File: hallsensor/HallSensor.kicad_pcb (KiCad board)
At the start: 2 copper layers, 6.3 x 20.3 mm, 5 parts

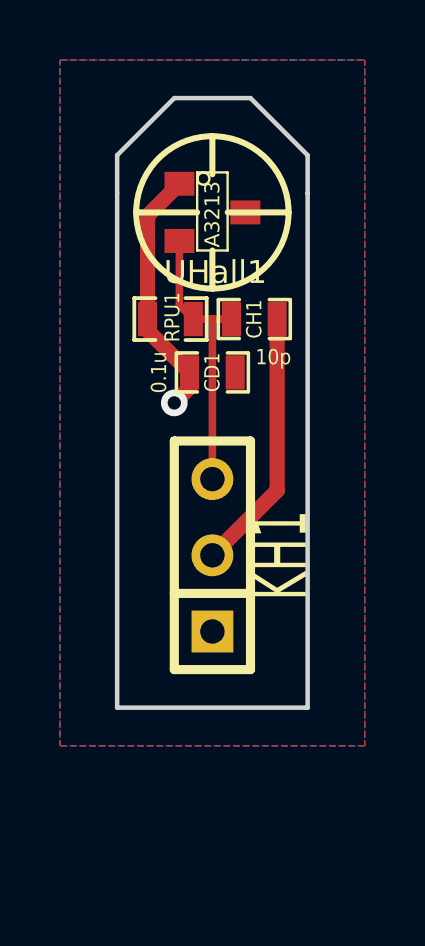
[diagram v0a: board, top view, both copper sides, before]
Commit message: Revised copper pour and and routing.
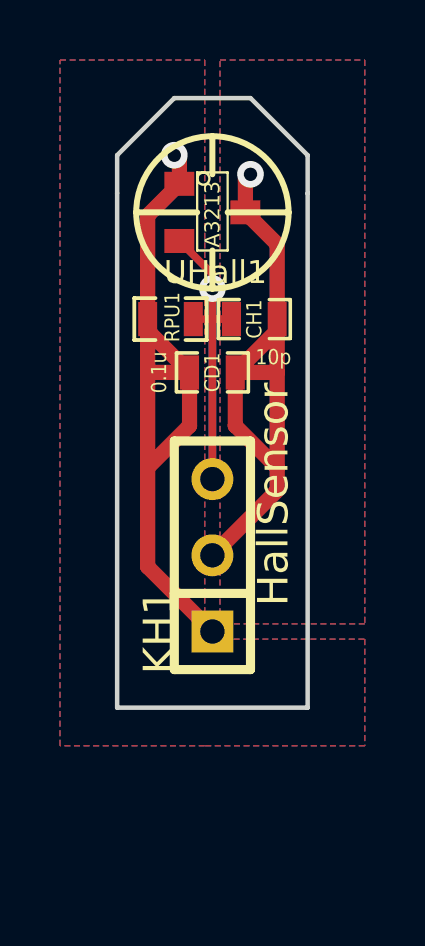
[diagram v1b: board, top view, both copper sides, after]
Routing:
- net VCC: track 8.53 -> 24.8 mm
- net VSS: track 8.77 -> 21.6 mm, vias 0 -> 1
- net /hall1: track 9.40 -> 16.0 mm, vias 0 -> 1
- added copper zone on F.Cu, net VCC
- added copper zone on B.Cu, net VSS
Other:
- board text added: "ClothBot Designs"
- board text added: "HallSensor"

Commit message: Added alignment vias at +/-0.1"
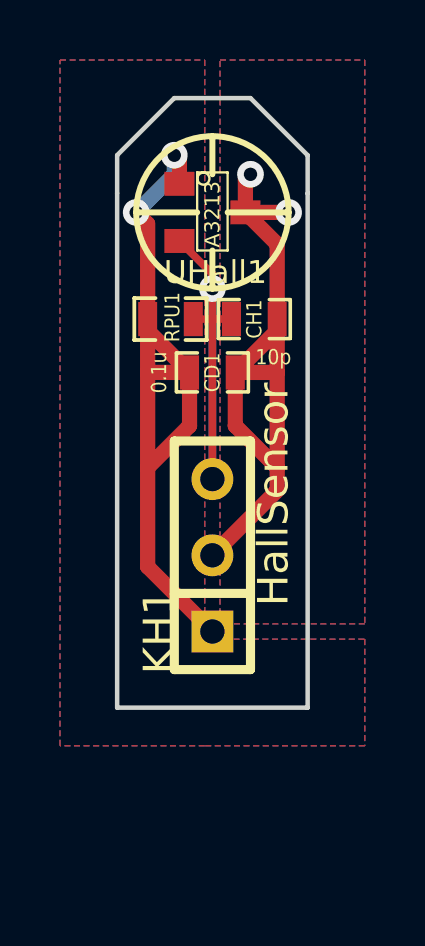
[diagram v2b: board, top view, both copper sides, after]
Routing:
- net VSS: track 21.6 -> 23.1 mm, vias 1 -> 2
- net VCC: track 24.8 -> 26.0 mm, vias 1 -> 2
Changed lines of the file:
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@@
-(kicad_pcb (version 3) (host pcbnew "(2013-09-28 BZR 4356)-product")
+(kicad_pcb (version 3) (host pcbnew "(2013-mar-25)-stable")
   (general
     (links 9)
     (no_connects 0)
-    (area 11.059524 17.610001 30.480001 43.180001)
+    (area 11.059524 17.610001 31.62179 43.180001)
     (thickness 1.6)
     (drawings 20)
-    (tracks 36)
+    (tracks 41)
     (zones 0)
     (modules 5)
@@
   (layers
     (15 F.Cu signal)
-    (0 B.Cu signal)
+    (0 B.Cu signal hide)
     (16 B.Adhes user)
     (17 F.Adhes user)
@@
       (usegerberextensions true)
       (excludeedgelayer true)
-      (linewidth 0.150000)
+      (linewidth 0)
       (plotframeref false)
       (viasonmask false)
@@
     (fp_line (start 1.27 0.508) (end -1.3335 0.508) (layer F.SilkS) (width 0.07874))
     (fp_line (start -1.3335 -0.508) (end 1.27 -0.508) (layer F.SilkS) (width 0.07874))
-    (pad 2 smd rect (at 0 -1.09982 270) (size 0.8001 1.00076) (layers F.Cu F.Paste F.Mask)
-      (net 3 VSS))
-    (pad 3 smd rect (at 0.9525 1.09982 270) (size 0.8001 1.00076) (layers F.Cu F.Paste F.Mask)
-      (net 1 /hall1))
-    (pad 1 smd rect (at -0.9525 1.09982 270) (size 0.8001 1.00076) (layers F.Cu F.Paste F.Mask)
-      (net 2 VCC))
+    (pad 2 smd rect (at 0 -1.09982 270) (size 0.8001 1.00076)
+      (layers F.Cu F.Paste F.Mask)
+      (net 3 VSS)
+    )
+    (pad 3 smd rect (at 0.9525 1.09982 270) (size 0.8001 1.00076)
+      (layers F.Cu F.Paste F.Mask)
+      (net 1 /hall1)
+    )
+    (pad 1 smd rect (at -0.9525 1.09982 270) (size 0.8001 1.00076)
+      (layers F.Cu F.Paste F.Mask)
+      (net 2 VCC)
+    )
     (model smd\SOT23_3.wrl
       (at (xyz 0 0 0))
@@
     (fp_line (start 1.19888 -0.635) (end 1.19888 0.635) (layer F.SilkS) (width 0.11938))
     (fp_line (start -1.19888 0.635) (end -1.19888 -0.635) (layer F.SilkS) (width 0.11938))
-    (pad 1 smd rect (at -0.762 0) (size 0.635 1.143) (layers F.Cu F.Paste F.Mask)
-      (net 2 VCC))
-    (pad 2 smd rect (at 0.762 0) (size 0.635 1.143) (layers F.Cu F.Paste F.Mask)
-      (net 3 VSS))
+    (pad 1 smd rect (at -0.762 0) (size 0.635 1.143)
+      (layers F.Cu F.Paste F.Mask)
+      (net 2 VCC)
+    )
+    (pad 2 smd rect (at 0.762 0) (size 0.635 1.143)
+      (layers F.Cu F.Paste F.Mask)
+      (net 3 VSS)
+    )
     (model smd\capacitors\C0603.wrl
       (at (xyz 0 0 0.001))
@@
     (fp_line (start 1.19888 -0.635) (end 1.19888 0.635) (layer F.SilkS) (width 0.11938))
     (fp_line (start -1.19888 0.635) (end -1.19888 -0.635) (layer F.SilkS) (width 0.11938))
-    (pad 1 smd rect (at -0.762 0) (size 0.635 1.143) (layers F.Cu F.Paste F.Mask)
-      (net 1 /hall1))
-    (pad 2 smd rect (at 0.762 0) (size 0.635 1.143) (layers F.Cu F.Paste F.Mask)
-      (net 3 VSS))
+    (pad 1 smd rect (at -0.762 0) (size 0.635 1.143)
+      (layers F.Cu F.Paste F.Mask)
+      (net 1 /hall1)
+    )
+    (pad 2 smd rect (at 0.762 0) (size 0.635 1.143)
+      (layers F.Cu F.Paste F.Mask)
+      (net 3 VSS)
+    )
     (model smd\capacitors\C0603.wrl
       (at (xyz 0 0 0.001))
@@
     (fp_line (start 3.81 1.27) (end -3.81 1.27) (layer F.SilkS) (width 0.3048))
     (fp_line (start -1.27 -1.27) (end -1.27 1.27) (layer F.SilkS) (width 0.3048))
-    (pad 1 thru_hole rect (at -2.54 0 90) (size 1.397 1.397) (drill 0.8128) (layers *.Cu *.Mask F.SilkS)
-      (net 2 VCC))
-    (pad 2 thru_hole circle (at 0 0 90) (size 1.397 1.397) (drill 0.8128) (layers *.Cu *.Mask F.SilkS)
-      (net 3 VSS))
-    (pad 3 thru_hole circle (at 2.54 0 90) (size 1.397 1.397) (drill 0.8128) (layers *.Cu *.Mask F.SilkS)
-      (net 1 /hall1))
+    (pad 1 thru_hole rect (at -2.54 0 90) (size 1.397 1.397) (drill 0.8128)
+      (layers *.Cu *.Mask F.SilkS)
+      (net 2 VCC)
+    )
+    (pad 2 thru_hole circle (at 0 0 90) (size 1.397 1.397) (drill 0.8128)
+      (layers *.Cu *.Mask F.SilkS)
+      (net 3 VSS)
+    )
+    (pad 3 thru_hole circle (at 2.54 0 90) (size 1.397 1.397) (drill 0.8128)
+      (layers *.Cu *.Mask F.SilkS)
+      (net 1 /hall1)
+    )
   )
   (module SM0603_Resistor (layer F.Cu)
@@
     (fp_line (start 1.2065 -0.6985) (end 1.2065 0.6985) (layer F.SilkS) (width 0.127))
     (fp_line (start 1.2065 0.6985) (end 0.50038 0.6985) (layer F.SilkS) (width 0.127))
-    (pad 1 smd rect (at -0.762 0) (size 0.635 1.143) (layers F.Cu F.Paste F.Mask)
-      (net 2 VCC))
-    (pad 2 smd rect (at 0.762 0) (size 0.635 1.143) (layers F.Cu F.Paste F.Mask)
-      (net 1 /hall1))
+    (pad 1 smd rect (at -0.762 0) (size 0.635 1.143)
+      (layers F.Cu F.Paste F.Mask)
+      (net 2 VCC)
+    )
+    (pad 2 smd rect (at 0.762 0) (size 0.635 1.143)
+      (layers F.Cu F.Paste F.Mask)
+      (net 1 /hall1)
+    )
     (model smd\resistors\R0603.wrl
       (at (xyz 0 0 0.001))
@@
   (segment (start 24.765 28.956) (end 25.4 28.956) (width 0.254) (layer F.Cu) (net 1))
   (segment (start 25.4 28.956) (end 26.035 28.956) (width 0.254) (layer F.Cu) (net 1))
+  (segment (start 24.13 23.495) (end 24.13 24.13) (width 0.508) (layer B.Cu) (net 2))
+  (segment (start 24.30018 23.66518) (end 24.13 23.495) (width 0.508) (layer F.Cu) (net 2))
+  (via (at 24.13 23.495) (size 0.889) (layers F.Cu B.Cu) (net 2))
   (segment (start 24.30018 24.4475) (end 24.30018 23.66518) (width 0.508) (layer F.Cu) (net 2))
-  (via (at 24.13 23.495) (size 0.889) (layers F.Cu B.Cu) (net 2))
-  (segment (start 24.30018 23.66518) (end 24.13 23.495) (width 0.508) (layer F.Cu) (net 2))
+  (segment (start 23.241 25.781) (end 22.86 25.4) (width 0.508) (layer F.Cu) (net 2))
+  (via (at 22.86 25.4) (size 0.889) (layers F.Cu B.Cu) (net 2))
+  (segment (start 23.241 25.781) (end 23.241 28.956) (width 0.508) (layer F.Cu) (net 2))
+  (segment (start 24.13 24.13) (end 22.86 25.4) (width 0.508) (layer B.Cu) (net 2))
   (segment (start 23.241 28.956) (end 23.241 29.337) (width 0.508) (layer F.Cu) (net 2))
   (segment (start 23.241 29.337) (end 24.638 30.734) (width 0.508) (layer F.Cu) (net 2))
@@
   (segment (start 23.241 33.909) (end 23.241 37.211) (width 0.508) (layer F.Cu) (net 2))
   (segment (start 23.241 37.211) (end 25.4 39.37) (width 0.508) (layer F.Cu) (net 2))
-  (segment (start 23.241 28.956) (end 23.241 25.50668) (width 0.508) (layer F.Cu) (net 2))
-  (segment (start 23.241 25.50668) (end 24.30018 24.4475) (width 0.508) (layer F.Cu) (net 2))
+  (segment (start 26.49982 25.4) (end 27.94 25.4) (width 0.508) (layer F.Cu) (net 3))
+  (via (at 27.94 25.4) (size 0.889) (layers F.Cu B.Cu) (net 3))
   (segment (start 26.49982 25.4) (end 26.49982 24.30018) (width 0.508) (layer F.Cu) (net 3))
   (via (at 26.67 24.13) (size 0.889) (layers F.Cu B.Cu) (net 3))

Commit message: Misc rework.
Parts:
- removed KH1: CONN_3, SIL-3
- added ANCHOR1: CONN_1, PINTST, F.Cu at (25.4, 22.9)
- added PAIR1: CONN_2, EDGE_2, F.Cu at (24.1, 38.1)
- added PAIR2: CONN_2, EDGE_2, F.Cu at (25.4, 38.1)
- added PAIR3: CONN_2, EDGE_2, F.Cu at (26.7, 38.1)
- moved CD1 0.64 mm to (25.4, 30.1)
- moved CH1 0.63 mm to (26.8, 28.3)
- moved RPU1 0.63 mm to (24.0, 28.3)
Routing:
- net /hall1: track 16.0 -> 23.1 mm, vias 1 -> 3
- net VCC: track 26.0 -> 23.7 mm, vias 2 -> 3
- net VSS: track 23.1 -> 22.8 mm, vias 2 -> 4
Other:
- net class Default: clearance 0.254 -> 0.2032
- net class PWR_Nets: clearance 0.254 -> 0.2032
- rule trace_clearance: 0.254 -> 0.2032

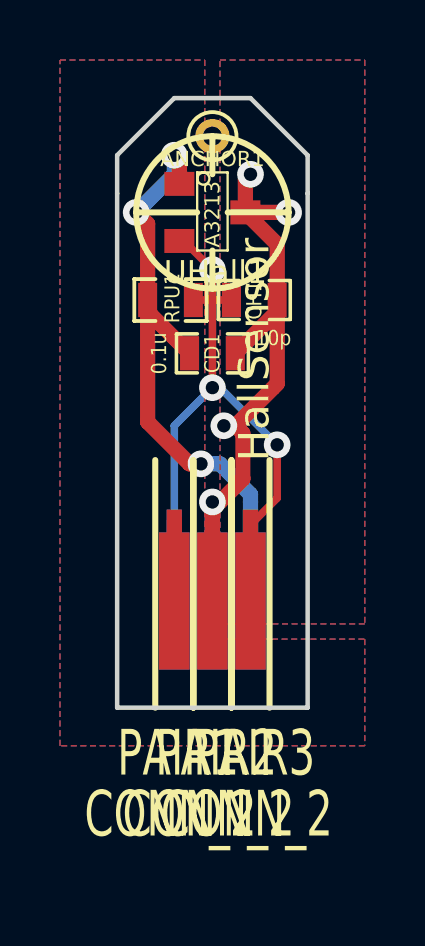
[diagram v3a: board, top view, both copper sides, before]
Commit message: Adjusted EDGE_2 silk layer.
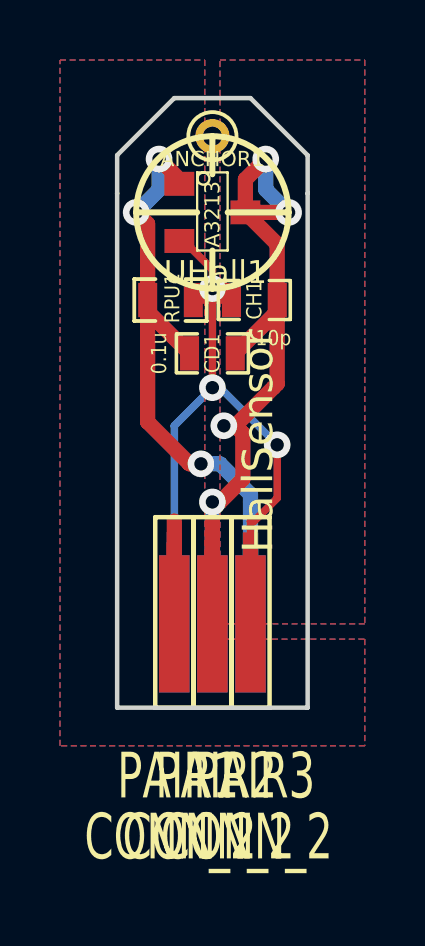
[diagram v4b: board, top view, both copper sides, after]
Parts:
- moved PAIR1 0.76 mm to (24.1, 38.9)
- moved PAIR2 0.76 mm to (25.4, 38.9)
- moved PAIR3 0.76 mm to (26.7, 38.9)
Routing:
- net VSS: track 22.8 -> 31.0 mm
- net /hall1: track 23.1 -> 28.7 mm
- net VCC: track 23.7 -> 28.8 mm
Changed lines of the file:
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@@
     (links 18)
     (no_connects 1)
-    (area 11.059524 17.610001 30.98679 46.5328)
+    (area 11.059524 17.610001 31.11379 47.2948)
     (thickness 1.6)
     (drawings 20)
-    (tracks 62)
+    (tracks 71)
     (zones 0)
     (modules 8)
@@
   )
   (module EDGE_2 (layer F.Cu)
-    (at 25.4 38.1 180)
+    (at 25.4 38.862 180)
     (descr "Edge Connector")
     (tags "EDGE CONN")
@@
       (effects (font (size 1.524 1.016) (thickness 0.2032)))
     )
-    (fp_line (start 0.635 4.445) (end 0.635 -3.81) (layer F.SilkS) (width 0.2032))
-    (fp_line (start -0.635 4.445) (end -0.635 -3.81) (layer F.SilkS) (width 0.2032))
+    (fp_line (start -0.635 3.302) (end 0.635 3.302) (layer F.SilkS) (width 0.15))
+    (fp_line (start 0.635 3.302) (end 0.635 -3.048) (layer F.SilkS) (width 0.15))
+    (fp_line (start 0.635 -3.048) (end -0.635 -3.048) (layer F.SilkS) (width 0.15))
+    (fp_line (start -0.635 -3.048) (end -0.635 3.302) (layer F.SilkS) (width 0.15))
     (pad 1 connect rect (at 0 -0.254 180) (size 1.016 4.572)
       (layers F.Cu F.Mask)
@@
   )
   (module EDGE_2 (layer F.Cu)
-    (at 26.67 38.1 180)
+    (at 26.67 38.862 180)
     (descr "Edge Connector")
     (tags "EDGE CONN")
@@
       (effects (font (size 1.524 1.016) (thickness 0.2032)))
     )
-    (fp_line (start 0.635 4.445) (end 0.635 -3.81) (layer F.SilkS) (width 0.2032))
-    (fp_line (start -0.635 4.445) (end -0.635 -3.81) (layer F.SilkS) (width 0.2032))
+    (fp_line (start -0.635 3.302) (end 0.635 3.302) (layer F.SilkS) (width 0.15))
+    (fp_line (start 0.635 3.302) (end 0.635 -3.048) (layer F.SilkS) (width 0.15))
+    (fp_line (start 0.635 -3.048) (end -0.635 -3.048) (layer F.SilkS) (width 0.15))
+    (fp_line (start -0.635 -3.048) (end -0.635 3.302) (layer F.SilkS) (width 0.15))
     (pad 1 connect rect (at 0 -0.254 180) (size 1.016 4.572)
       (layers F.Cu F.Mask)
@@
   )
   (module EDGE_2 (layer F.Cu)
-    (at 24.13 38.1 180)
+    (at 24.13 38.862 180)
     (descr "Edge Connector")
     (tags "EDGE CONN")
@@
       (effects (font (size 1.524 1.016) (thickness 0.2032)))
     )
-    (fp_line (start 0.635 4.445) (end 0.635 -3.81) (layer F.SilkS) (width 0.2032))
-    (fp_line (start -0.635 4.445) (end -0.635 -3.81) (layer F.SilkS) (width 0.2032))
+    (fp_line (start -0.635 3.302) (end 0.635 3.302) (layer F.SilkS) (width 0.15))
+    (fp_line (start 0.635 3.302) (end 0.635 -3.048) (layer F.SilkS) (width 0.15))
+    (fp_line (start 0.635 -3.048) (end -0.635 -3.048) (layer F.SilkS) (width 0.15))
+    (fp_line (start -0.635 -3.048) (end -0.635 3.302) (layer F.SilkS) (width 0.15))
     (pad 1 connect rect (at 0 -0.254 180) (size 1.016 4.572)
       (layers F.Cu F.Mask)
@@
     )
   )
-  (gr_text "ClothBot Designs" (at 23.622 33.274 90) (layer B.SilkS)
+  (gr_text "ClothBot Designs" (at 23.876 30.226 90) (layer B.SilkS)
     (effects (font (size 1.016 1.016) (thickness 0.2032)) (justify mirror))
   )
-  (gr_text HallSensor (at 26.797 29.972 90) (layer F.SilkS)
+  (gr_text HallSensor (at 26.924 33.02 90) (layer F.SilkS)
     (effects (font (size 1.016 1.016) (thickness 0.2032)))
   )
@@
   (gr_circle (center 25.4 25.4) (end 27.94 25.4) (layer B.SilkS) (width 0.2))
   (gr_circle (center 25.4 25.4) (end 27.94 25.4) (layer F.SilkS) (width 0.2))
+  (segment (start 25.4 28.194) (end 25.4 27.94) (width 0.254) (layer F.Cu) (net 1))
+  (via (at 25.4 27.94) (size 0.889) (layers F.Cu B.Cu) (net 1))
+  (segment (start 26.67 36.449) (end 26.67 39.116) (width 0.254) (layer F.Cu) (net 1))
+  (segment (start 24.13 36.449) (end 24.13 39.116) (width 0.254) (layer B.Cu) (net 1))
   (segment (start 27.559 33.147) (end 25.654 31.242) (width 0.254) (layer B.Cu) (net 1))
   (segment (start 26.67 35.687) (end 26.67 38.354) (width 0.254) (layer F.Cu) (net 1))
@@
   (segment (start 25.4 28.194) (end 25.4 27.305) (width 0.254) (layer F.Cu) (net 1))
   (segment (start 24.4475 26.3525) (end 25.4 27.305) (width 0.254) (layer F.Cu) (net 1))
-  (via (at 25.4 27.305) (size 0.889) (layers F.Cu B.Cu) (net 1))
   (segment (start 24.4475 26.3525) (end 24.30018 26.3525) (width 0.254) (layer F.Cu) (net 1))
   (segment (start 24.765 28.321) (end 25.4 28.321) (width 0.254) (layer F.Cu) (net 1))
   (segment (start 25.4 28.321) (end 26.035 28.321) (width 0.254) (layer F.Cu) (net 1))
+  (segment (start 23.622 23.622) (end 23.622 24.638) (width 0.508) (layer B.Cu) (net 2))
+  (via (at 22.86 25.4) (size 0.889) (layers F.Cu B.Cu) (net 2))
+  (segment (start 23.241 25.781) (end 22.86 25.4) (width 0.508) (layer F.Cu) (net 2))
+  (segment (start 23.241 28.321) (end 23.241 25.781) (width 0.508) (layer F.Cu) (net 2))
+  (segment (start 24.30018 24.30018) (end 23.622 23.622) (width 0.508) (layer F.Cu) (net 2))
+  (via (at 23.622 23.622) (size 0.889) (layers F.Cu B.Cu) (net 2))
+  (segment (start 24.30018 24.30018) (end 24.30018 24.4475) (width 0.508) (layer F.Cu) (net 2))
+  (segment (start 23.622 24.638) (end 22.86 25.4) (width 0.508) (layer B.Cu) (net 2))
+  (segment (start 24.13 36.449) (end 24.13 39.116) (width 0.508) (layer F.Cu) (net 2))
+  (segment (start 26.67 36.449) (end 26.67 39.116) (width 0.508) (layer B.Cu) (net 2))
+  (segment (start 24.13 35.687) (end 24.13 38.354) (width 0.508) (layer F.Cu) (net 2))
   (segment (start 25.019 33.782) (end 25.654 33.782) (width 0.508) (layer B.Cu) (net 2))
   (segment (start 26.67 35.052) (end 26.67 35.687) (width 0.508) (layer B.Cu) (net 2))
   (segment (start 26.67 34.798) (end 26.67 35.052) (width 0.508) (layer B.Cu) (net 2))
   (segment (start 25.654 33.782) (end 26.67 34.798) (width 0.508) (layer B.Cu) (net 2))
-  (segment (start 24.13 35.687) (end 24.13 38.354) (width 0.508) (layer F.Cu) (net 2))
   (segment (start 26.67 35.687) (end 26.67 38.354) (width 0.508) (layer B.Cu) (net 2))
   (segment (start 23.241 32.385) (end 24.638 33.782) (width 0.508) (layer F.Cu) (net 2))
@@
   (segment (start 23.241 28.321) (end 23.241 28.702) (width 0.508) (layer F.Cu) (net 2))
   (segment (start 23.241 28.702) (end 24.638 30.099) (width 0.508) (layer F.Cu) (net 2))
-  (segment (start 23.241 28.321) (end 23.241 25.781) (width 0.508) (layer F.Cu) (net 2))
-  (segment (start 24.13 24.13) (end 22.86 25.4) (width 0.508) (layer B.Cu) (net 2))
-  (via (at 22.86 25.4) (size 0.889) (layers F.Cu B.Cu) (net 2))
-  (segment (start 23.241 25.781) (end 22.86 25.4) (width 0.508) (layer F.Cu) (net 2))
-  (segment (start 24.30018 23.66518) (end 24.30018 24.4475) (width 0.508) (layer F.Cu) (net 2))
-  (via (at 24.13 23.495) (size 0.889) (layers F.Cu B.Cu) (net 2))
-  (segment (start 24.30018 23.66518) (end 24.13 23.495) (width 0.508) (layer F.Cu) (net 2))
-  (segment (start 24.13 23.495) (end 24.13 24.13) (width 0.508) (layer B.Cu) (net 2))
+  (segment (start 27.178 23.622) (end 27.178 24.638) (width 0.508) (layer B.Cu) (net 3))
+  (via (at 27.94 25.4) (size 0.889) (layers F.Cu B.Cu) (net 3))
+  (segment (start 26.49982 25.4) (end 27.94 25.4) (width 0.508) (layer F.Cu) (net 3))
+  (segment (start 26.49982 24.30018) (end 27.178 23.622) (width 0.508) (layer F.Cu) (net 3))
+  (via (at 27.178 23.622) (size 0.889) (layers F.Cu B.Cu) (net 3))
+  (segment (start 26.49982 25.4) (end 26.49982 24.30018) (width 0.508) (layer F.Cu) (net 3))
+  (segment (start 27.178 24.638) (end 27.94 25.4) (width 0.508) (layer B.Cu) (net 3))
+  (segment (start 25.4 36.449) (end 25.4 39.116) (width 0.508) (layer F.Cu) (net 3))
+  (segment (start 25.4 36.449) (end 25.4 39.116) (width 0.508) (layer B.Cu) (net 3))
   (segment (start 25.4 35.687) (end 25.4 38.354) (width 0.508) (layer F.Cu) (net 3))
   (segment (start 25.4 35.687) (end 25.4 38.354) (width 0.508) (layer B.Cu) (net 3))
@@
   (segment (start 27.559 28.321) (end 27.559 26.45918) (width 0.508) (layer F.Cu) (net 3))
   (segment (start 27.559 26.45918) (end 26.49982 25.4) (width 0.508) (layer F.Cu) (net 3))
-  (segment (start 26.49982 25.4) (end 27.94 25.4) (width 0.508) (layer F.Cu) (net 3))
-  (via (at 27.94 25.4) (size 0.889) (layers F.Cu B.Cu) (net 3))
-  (segment (start 26.49982 25.4) (end 26.49982 24.30018) (width 0.508) (layer F.Cu) (net 3))
-  (via (at 26.67 24.13) (size 0.889) (layers F.Cu B.Cu) (net 3))
-  (segment (start 26.49982 24.30018) (end 26.67 24.13) (width 0.508) (layer F.Cu) (net 3))
   (zone (net 3) (net_name VSS) (layer F.Cu) (hatch edge 0.508)
     (connect_pads yes (clearance 0.381))

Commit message: Tweaked copper pour & via placement.
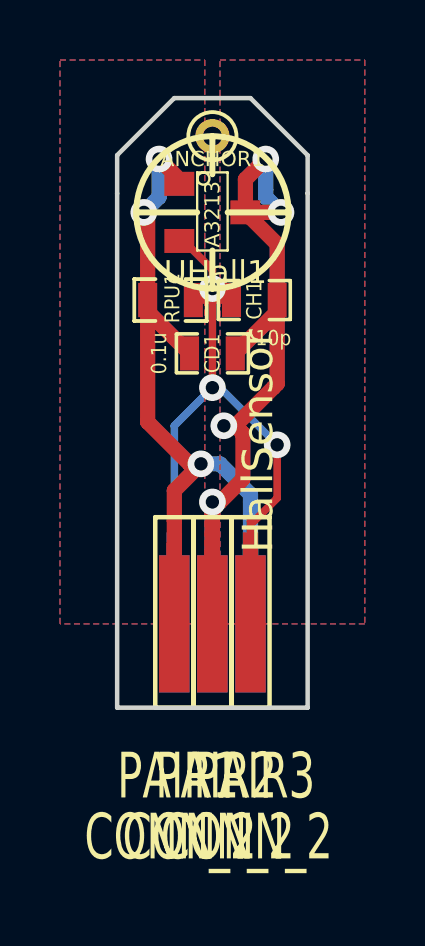
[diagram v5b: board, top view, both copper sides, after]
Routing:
- net VSS: track 31.0 -> 40.1 mm
- net VCC: track 28.8 -> 30.9 mm
